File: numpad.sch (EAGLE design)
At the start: 1 part, among them U1 PROMICRO

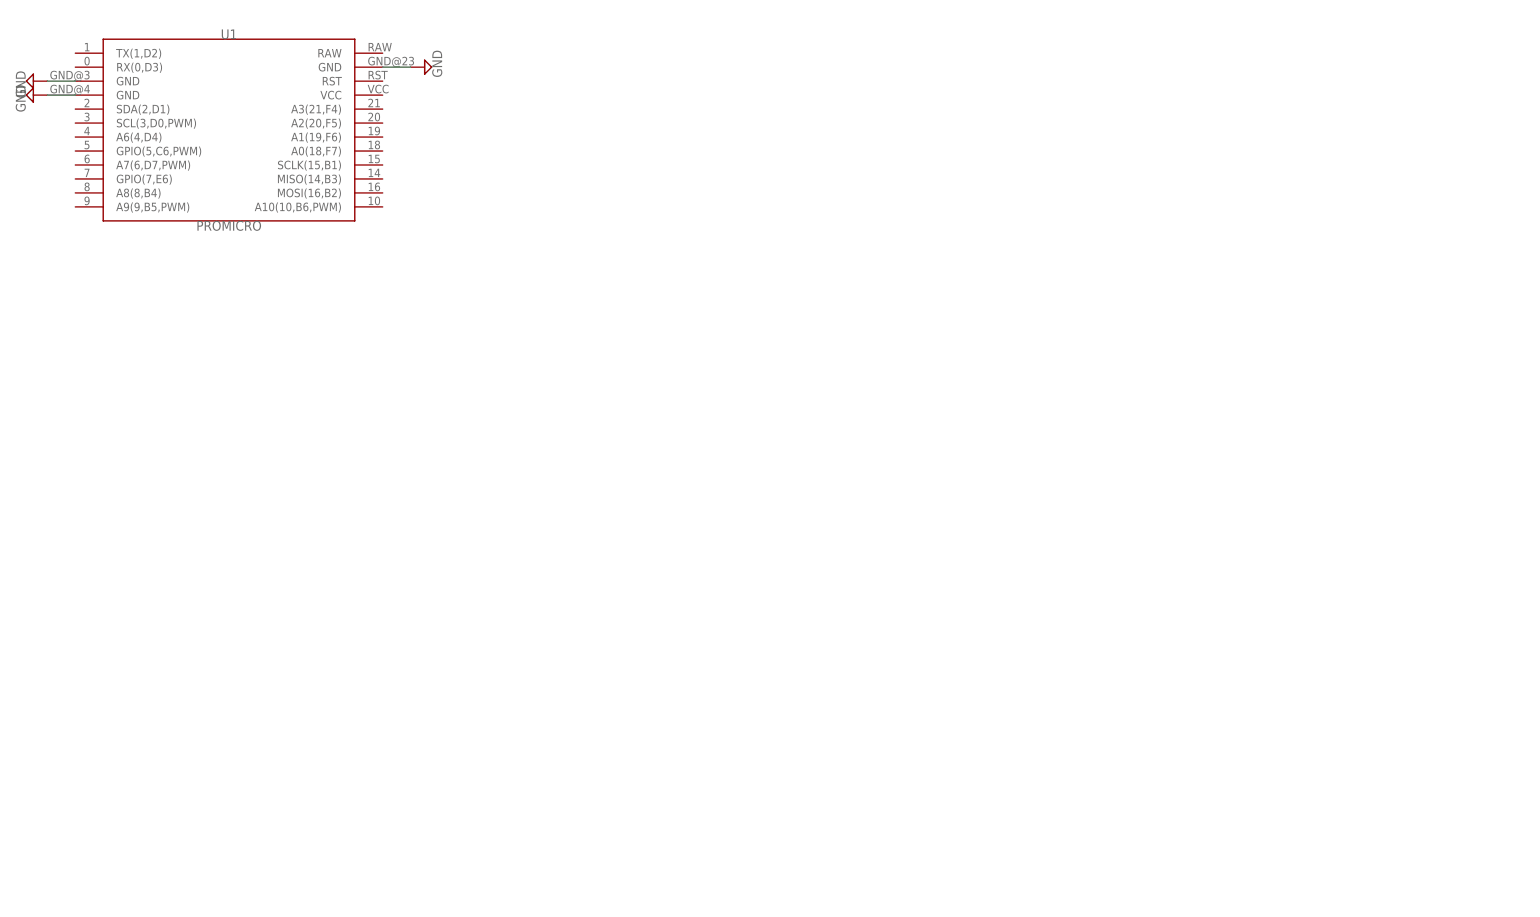
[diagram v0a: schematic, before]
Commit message: added switches and dxf of layout
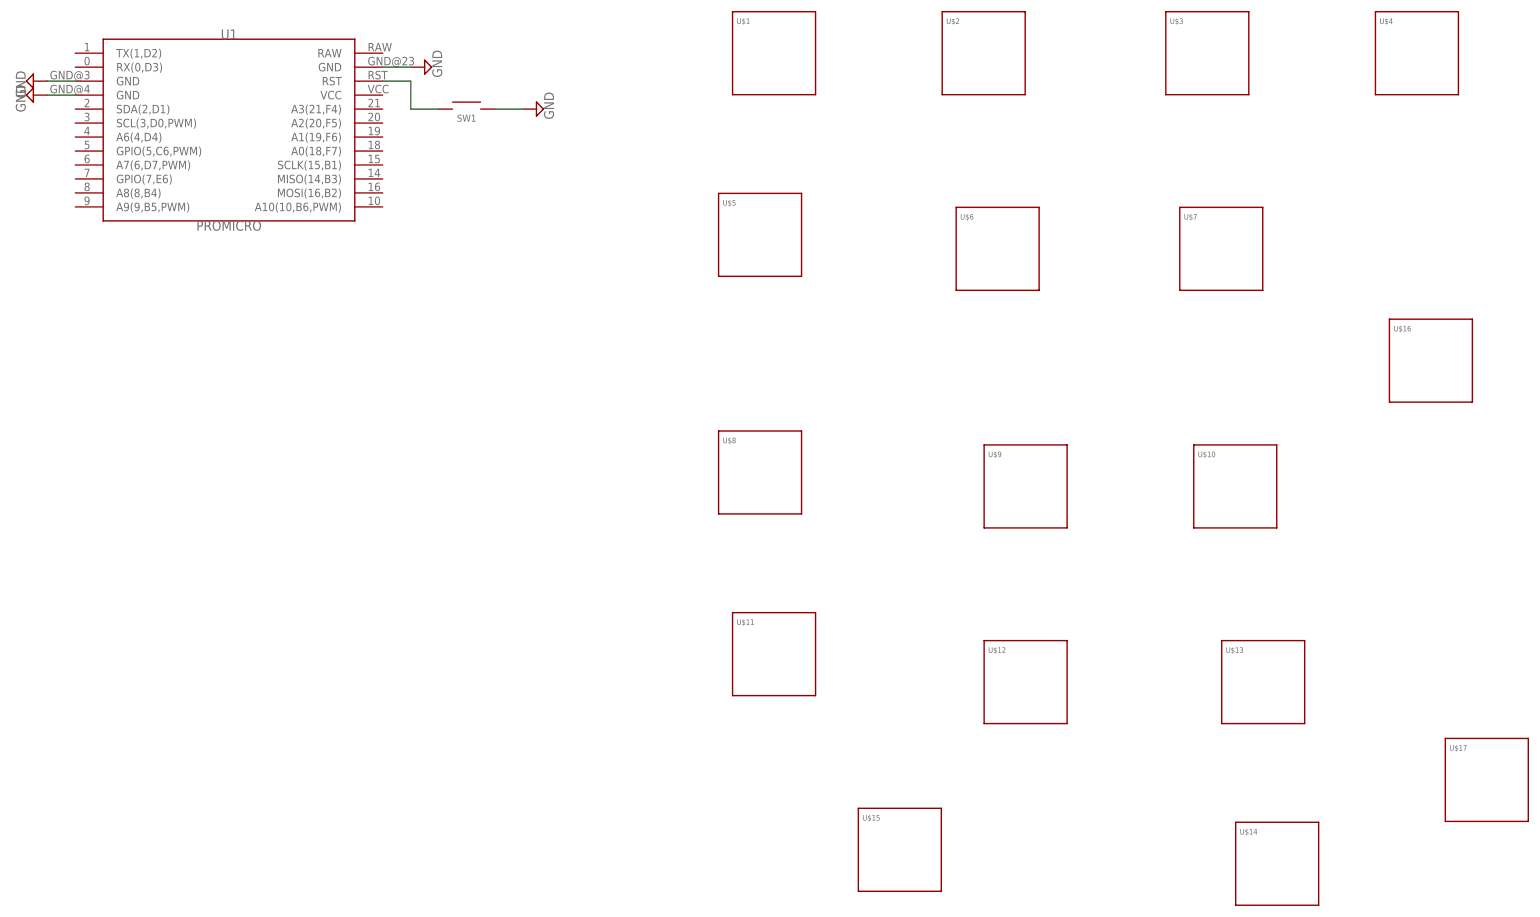
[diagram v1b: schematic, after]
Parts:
- added SW1: SWITCH-SMD-SCHURTER-1241.1612.11, Hardware:SWITCH-SMD-SCHURTER-1241.1612.11
- added U$1, U$10, U$11, U$12, U$13, U$14, U$2, U$3, U$4, U$5, U$6, U$7, U$8, U$9: KEYSWITCH-PLATE-MXPLATE-1U, Keyboard:KEYSWITCH-PLATE-MXPLATE-1U
- added U$15: KEYSWITCH-PLATE-MXPLATE-2U, Keyboard:KEYSWITCH-PLATE-MXPLATE-2U
- added U$16, U$17: KEYSWITCH-PLATE-MXPLATE-2U-ROTATED, Keyboard:KEYSWITCH-PLATE-MXPLATE-2U-ROTATED
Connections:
- new net N$1: SW1.1, U1.RST
- net GND: now also SW1.2
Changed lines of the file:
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@@
 <part name="SUPPLY2" library="supply2" library_urn="urn:adsk.eagle:library:372" deviceset="GND" device=""/>
 <part name="SUPPLY3" library="supply2" library_urn="urn:adsk.eagle:library:372" deviceset="GND" device=""/>
+<part name="U$1" library="Keyboard" deviceset="KEYSWITCH-PLATE" device="-MXPLATE-1U"/>
+<part name="U$2" library="Keyboard" deviceset="KEYSWITCH-PLATE" device="-MXPLATE-1U"/>
+<part name="U$3" library="Keyboard" deviceset="KEYSWITCH-PLATE" device="-MXPLATE-1U"/>
+<part name="U$4" library="Keyboard" deviceset="KEYSWITCH-PLATE" device="-MXPLATE-1U"/>
+<part name="U$5" library="Keyboard" deviceset="KEYSWITCH-PLATE" device="-MXPLATE-1U"/>
+<part name="U$6" library="Keyboard" deviceset="KEYSWITCH-PLATE" device="-MXPLATE-1U"/>
+<part name="U$7" library="Keyboard" deviceset="KEYSWITCH-PLATE" device="-MXPLATE-1U"/>
+<part name="U$8" library="Keyboard" deviceset="KEYSWITCH-PLATE" device="-MXPLATE-1U"/>
+<part name="U$9" library="Keyboard" deviceset="KEYSWITCH-PLATE" device="-MXPLATE-1U"/>
+<part name="U$10" library="Keyboard" deviceset="KEYSWITCH-PLATE" device="-MXPLATE-1U"/>
+<part name="U$11" library="Keyboard" deviceset="KEYSWITCH-PLATE" device="-MXPLATE-1U"/>
+<part name="U$12" library="Keyboard" deviceset="KEYSWITCH-PLATE" device="-MXPLATE-1U"/>
+<part name="U$13" library="Keyboard" deviceset="KEYSWITCH-PLATE" device="-MXPLATE-1U"/>
+<part name="U$14" library="Keyboard" deviceset="KEYSWITCH-PLATE" device="-MXPLATE-1U"/>
+<part name="U$15" library="Keyboard" deviceset="KEYSWITCH-PLATE" device="-MXPLATE-2U"/>
+<part name="U$16" library="Keyboard" deviceset="KEYSWITCH-PLATE" device="-MXPLATE-2U-ROTATED"/>
+<part name="U$17" library="Keyboard" deviceset="KEYSWITCH-PLATE" device="-MXPLATE-2U-ROTATED"/>
+<part name="SW1" library="Hardware" deviceset="SWITCH-SMD" device="-SCHURTER-1241.1612.11"/>
+<part name="SUPPLY4" library="supply2" library_urn="urn:adsk.eagle:library:372" deviceset="GND" device=""/>
 </parts>
 <sheets>
@@
 <attribute name="VALUE" x="34.925" y="32.385" size="1.778" layer="96" rot="R270"/>
 </instance>
+<instance part="U$1" gate="G$1" x="172.72" y="38.1" smashed="yes">
+<attribute name="NAME" x="165.91" y="43.418" size="1" layer="95"/>
+</instance>
+<instance part="U$2" gate="G$1" x="210.82" y="38.1" smashed="yes">
+<attribute name="NAME" x="204.01" y="43.418" size="1" layer="95"/>
+</instance>
+<instance part="U$3" gate="G$1" x="251.46" y="38.1" smashed="yes">
+<attribute name="NAME" x="244.65" y="43.418" size="1" layer="95"/>
+</instance>
+<instance part="U$4" gate="G$1" x="289.56" y="38.1" smashed="yes">
+<attribute name="NAME" x="282.75" y="43.418" size="1" layer="95"/>
+</instance>
+<instance part="U$5" gate="G$1" x="170.18" y="5.08" smashed="yes">
+<attribute name="NAME" x="163.37" y="10.398" size="1" layer="95"/>
+</instance>
+<instance part="U$6" gate="G$1" x="213.36" y="2.54" smashed="yes">
+<attribute name="NAME" x="206.55" y="7.858" size="1" layer="95"/>
+</instance>
+<instance part="U$7" gate="G$1" x="254" y="2.54" smashed="yes">
+<attribute name="NAME" x="247.19" y="7.858" size="1" layer="95"/>
+</instance>
+<instance part="U$8" gate="G$1" x="170.18" y="-38.1" smashed="yes">
+<attribute name="NAME" x="163.37" y="-32.782" size="1" layer="95"/>
+</instance>
+<instance part="U$9" gate="G$1" x="218.44" y="-40.64" smashed="yes">
+<attribute name="NAME" x="211.63" y="-35.322" size="1" layer="95"/>
+</instance>
+<instance part="U$10" gate="G$1" x="256.54" y="-40.64" smashed="yes">
+<attribute name="NAME" x="249.73" y="-35.322" size="1" layer="95"/>
+</instance>
+<instance part="U$11" gate="G$1" x="172.72" y="-71.12" smashed="yes">
+<attribute name="NAME" x="165.91" y="-65.802" size="1" layer="95"/>
+</instance>
+<instance part="U$12" gate="G$1" x="218.44" y="-76.2" smashed="yes">
+<attribute name="NAME" x="211.63" y="-70.882" size="1" layer="95"/>
+</instance>
+<instance part="U$13" gate="G$1" x="261.62" y="-76.2" smashed="yes">
+<attribute name="NAME" x="254.81" y="-70.882" size="1" layer="95"/>
+</instance>
+<instance part="U$14" gate="G$1" x="264.16" y="-109.22" smashed="yes">
+<attribute name="NAME" x="257.35" y="-103.902" size="1" layer="95"/>
+</instance>
+<instance part="U$15" gate="G$1" x="195.58" y="-106.68" smashed="yes">
+<attribute name="NAME" x="188.77" y="-101.362" size="1" layer="95"/>
+</instance>
+<instance part="U$16" gate="G$1" x="292.1" y="-17.78" smashed="yes">
+<attribute name="NAME" x="285.29" y="-12.462" size="1" layer="95"/>
+</instance>
+<instance part="U$17" gate="G$1" x="302.26" y="-93.98" smashed="yes">
+<attribute name="NAME" x="295.45" y="-88.662" size="1" layer="95"/>
+</instance>
+<instance part="SW1" gate="G$1" x="116.84" y="27.94" smashed="yes">
+<attribute name="NAME" x="116.84" y="25.654" size="1.27" layer="95" align="bottom-center"/>
+</instance>
+<instance part="SUPPLY4" gate="GND" x="129.54" y="27.94" smashed="yes" rot="R90">
+<attribute name="VALUE" x="132.715" y="26.035" size="1.778" layer="96" rot="R90"/>
+</instance>
 </instances>
 <busses>
@@
 <wire x1="101.6" y1="35.56" x2="106.68" y2="35.56" width="0.1524" layer="91"/>
 </segment>
+<segment>
+<pinref part="SW1" gate="G$1" pin="2"/>
+<pinref part="SUPPLY4" gate="GND" pin="GND"/>
+<wire x1="121.92" y1="27.94" x2="127" y2="27.94" width="0.1524" layer="91"/>
+</segment>
 </net>
+<net name="N$1" class="0">
+<segment>
+<pinref part="SW1" gate="G$1" pin="1"/>
+<wire x1="111.76" y1="27.94" x2="106.68" y2="27.94" width="0.1524" layer="91"/>
+<wire x1="106.68" y1="27.94" x2="106.68" y2="33.02" width="0.1524" layer="91"/>
+<pinref part="U1" gate="G$1" pin="RST"/>
+<wire x1="106.68" y1="33.02" x2="101.6" y2="33.02" width="0.1524" layer="91"/>
+</segment>
+</net>
